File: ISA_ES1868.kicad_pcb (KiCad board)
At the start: 4 copper layers, 104.1 x 99.1 mm, 105 parts, among them J1 LINE IN, J10 Vol. Btns, J11 ISA BUS, J2 LINE OUT, J3 Joystick/MIDI, J5 Wavetable, J7 SPKR OUT, J8 MIC IN, U1 L78L05, U2 74LS138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

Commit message: Fixed silkscreen text
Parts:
- JP3: value ~DRQ2~ Jumper -> DRQ2 Jumper

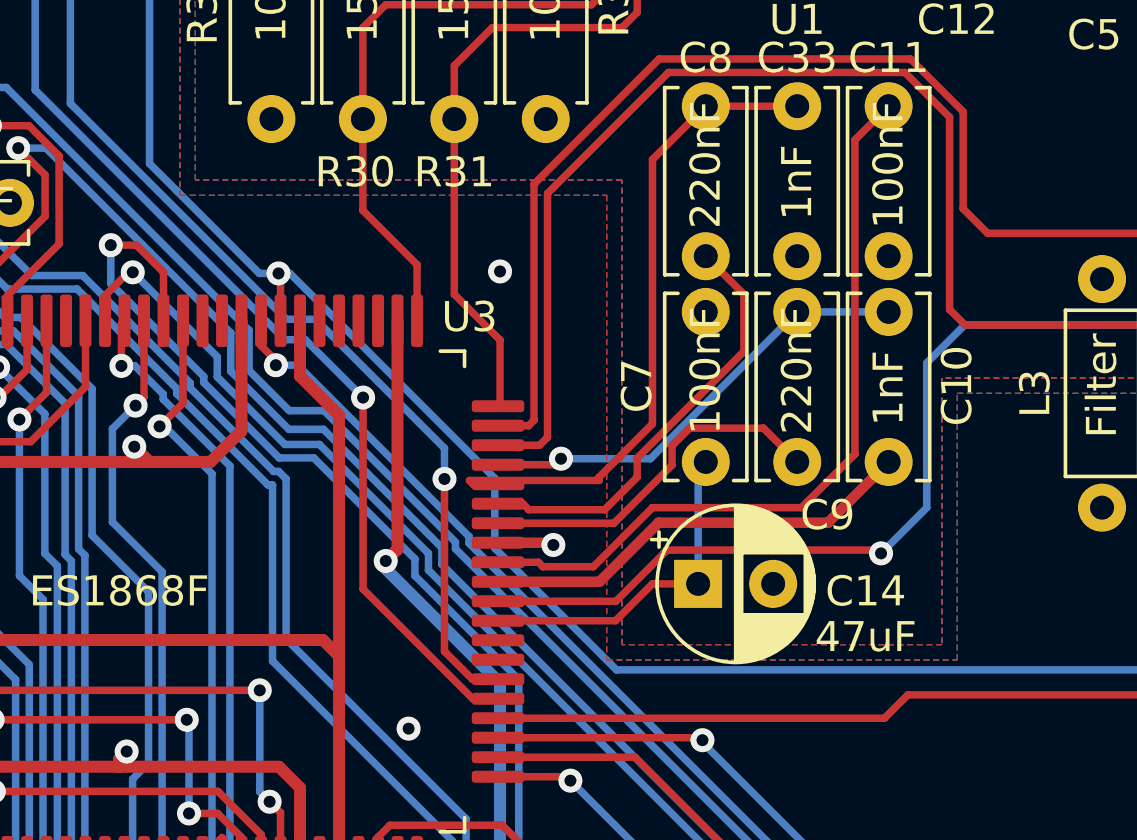
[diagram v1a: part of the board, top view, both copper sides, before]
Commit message: changed analog ground zone
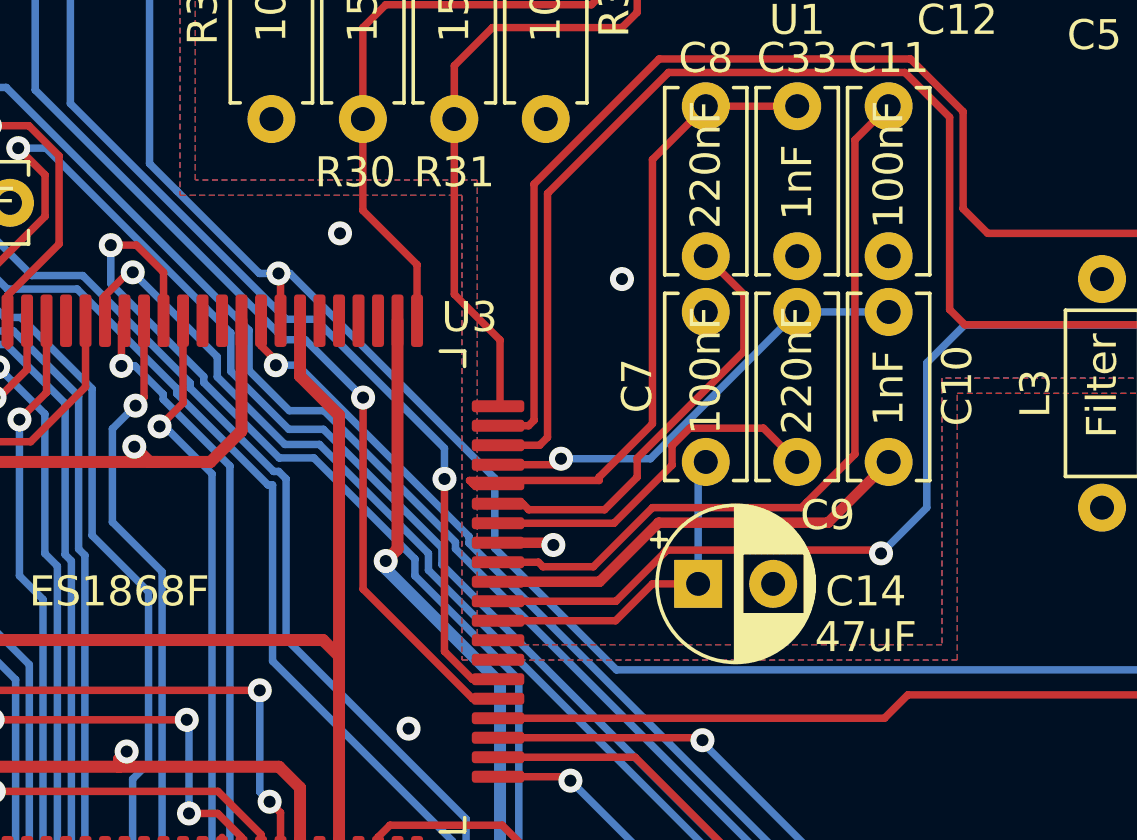
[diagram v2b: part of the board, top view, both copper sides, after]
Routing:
- net GNDA: track 313.7 -> 315.4 mm, vias 2 -> 3
- net GND: track 701.7 -> 702.4 mm

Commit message: Update silkscreen
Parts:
- J5: value Wavetable -> WAVETABLE EXPANSION
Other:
- board text added: "ES1868F ISA8 bit Sound Card by Hkz"
- board text added: "Rev 1.0"
- board text removed: "ES1868F ISA8 bit Sound Card rev. 1.0 by Hkz"

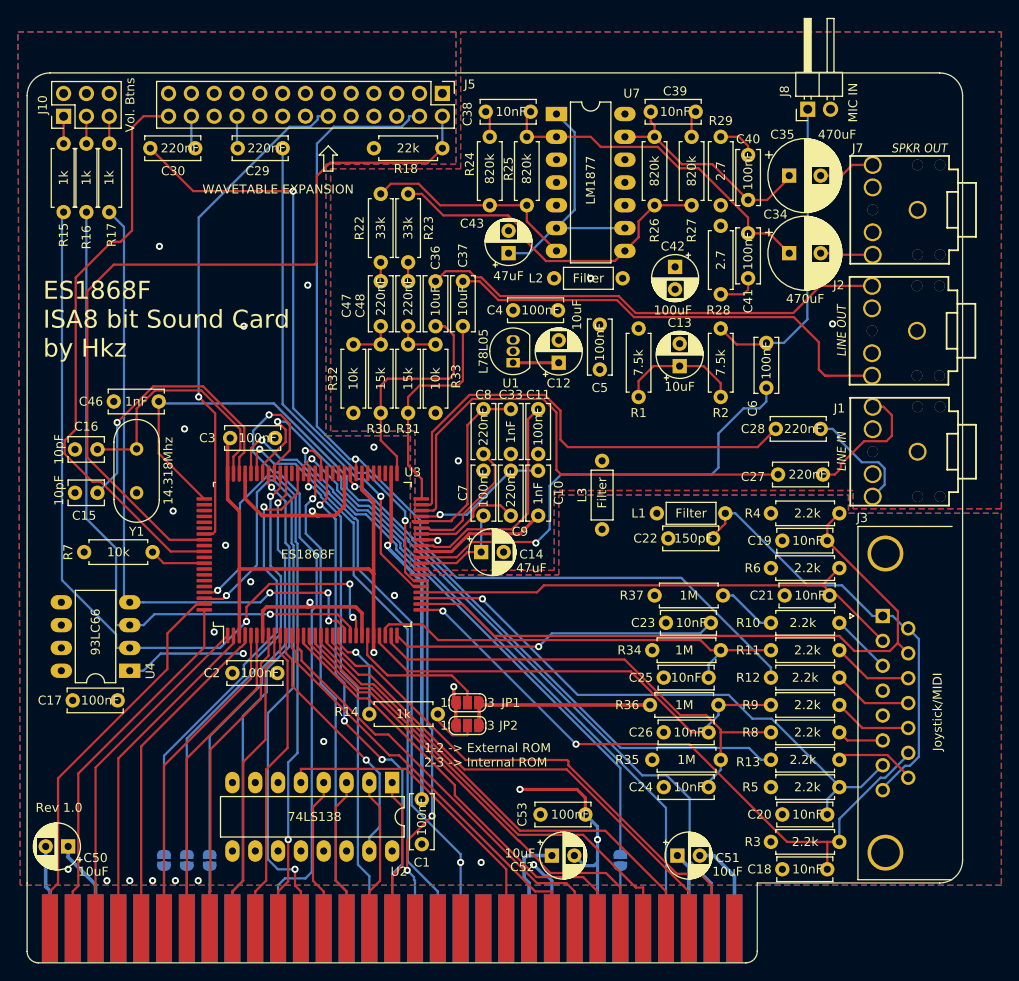
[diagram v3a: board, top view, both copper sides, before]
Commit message: Reorganized crystal on board and moved some traces
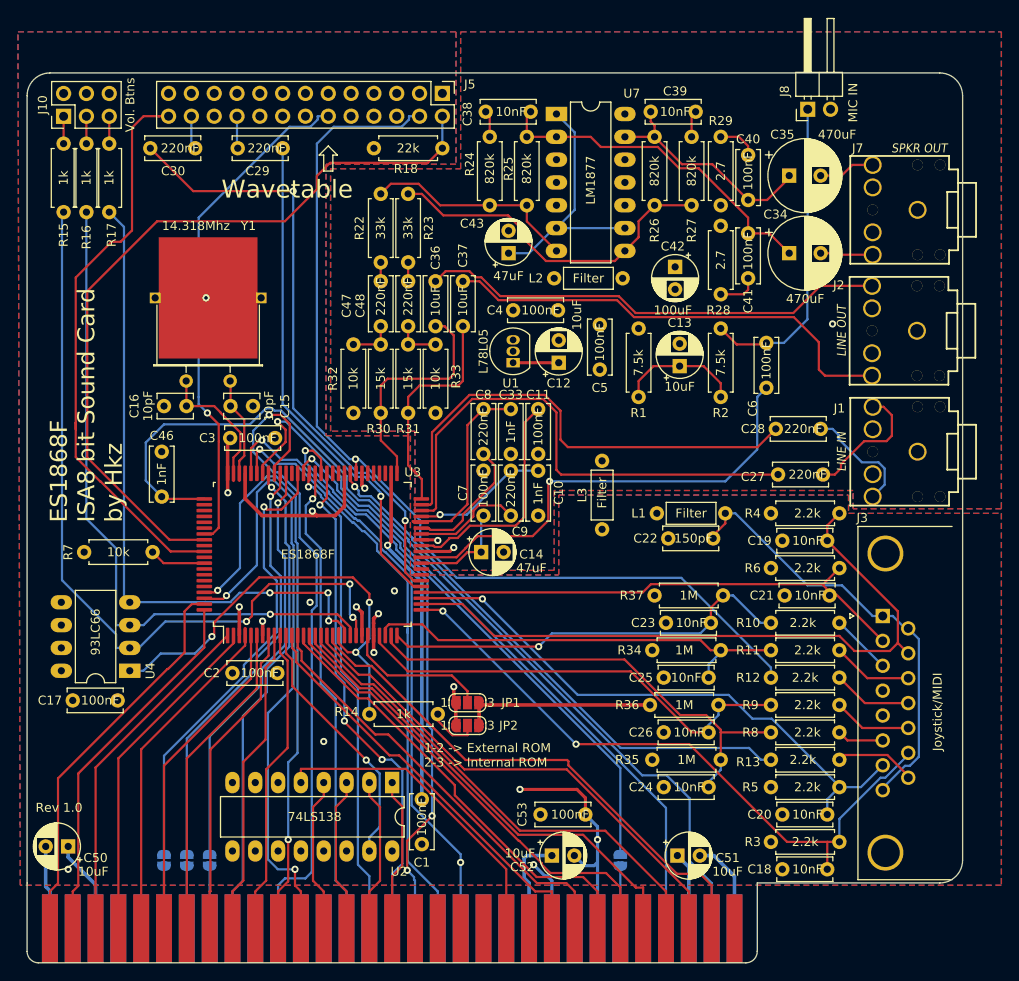
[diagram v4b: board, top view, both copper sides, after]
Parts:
- J5: value WAVETABLE EXPANSION -> Wavetable
- Y1: footprint Crystal:Crystal_HC49-4H_Vertical -> Crystal:Crystal_HC49-U_Horizontal_1EP_style2
- moved C15 22.0 mm to (236.0, 141.2), turned to 180 degrees
- moved Y1 16.2 mm to (233.4, 138.4), turned to 180 degrees
- moved C16 11.0 mm to (226.1, 141.2)
- moved C46 7.73 mm to (225.8, 146.3), turned to 270 degrees
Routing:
- net GND: track 702.4 -> 608.1 mm, vias 21 -> 9
- net Net-(C15-Pad2): track 37.0 -> 12.0 mm, vias 1 -> 0
- net Net-(R14-Pad2): track 37.5 -> 51.2 mm, vias 2 -> 3
- net Net-(C16-Pad2): track 29.1 -> 15.8 mm
- net GNDA: track 315.4 -> 303.6 mm, vias 3 -> 2
- net /MCLK: track 90.7 -> 85.9 mm
- net /RESETDRV: track 106.8 -> 108.1 mm
- net /A0: track 43.7 -> 44.9 mm
- net VCC: track 385.7 -> 384.9 mm, vias 2 -> 6
- net /A4: track 38.3 -> 39.1 mm
- net /~RSTB: track 64.8 -> 64.0 mm
- net Net-(C23-Pad2): track 46.8 -> 47.3 mm
- net /~IOR: track 65.8 -> 66.3 mm

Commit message: Slight change to traces, add gerbers
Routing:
- net GND: track 608.1 -> 629.0 mm, vias 9 -> 11
- net GNDA: track 303.6 -> 306.8 mm, vias 2 -> 3
- net /A3: track 37.9 -> 39.6 mm
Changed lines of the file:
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@@
     (thickness 1.6)
     (drawings 24)
-    (tracks 1401)
+    (tracks 1413)
     (zones 0)
     (modules 105)
@@
     (descr "Crystal THT HC-49/U http://5hertz.com/pdfs/04404_D.pdf")
     (tags "THT crystal")
-    (fp_text reference Y1 (at -2.032 17.272) (layer F.SilkS)
+    (fp_text reference Y1 (at -2.54 0) (layer F.SilkS)
       (effects (font (size 1 1) (thickness 0.15)))
     )
-    (fp_text value 14.318Mhz (at 3.81 17.272 180) (layer F.SilkS)
+    (fp_text value 14.318Mhz (at 9.906 8.89 270) (layer F.SilkS)
       (effects (font (size 1 1) (thickness 0.15)))
     )
@@
   (segment (start 280.162 174.498) (end 261.2081 174.498) (width 0.4) (layer F.Cu) (net 2) (status 30))
   (segment (start 261.2081 174.498) (end 261.142 174.4319) (width 0.4) (layer F.Cu) (net 2) (status 30))
-  (segment (start 216.154 153.416) (end 217.17 154.432) (width 0.4) (layer In1.Cu) (net 2))
-  (segment (start 217.17 154.432) (end 217.17 157.48) (width 0.4) (layer In1.Cu) (net 2) (status 20))
   (segment (start 214.63 165.608) (end 216.154 165.608) (width 0.4) (layer In1.Cu) (net 2) (status 10))
   (segment (start 216.154 165.608) (end 219.202 168.656) (width 0.4) (layer In1.Cu) (net 2))
@@
   (segment (start 249.428 112.522) (end 243.078 112.522) (width 0.4) (layer In1.Cu) (net 2) (status 10))
   (segment (start 243.078 112.522) (end 239.522 116.078) (width 0.4) (layer In1.Cu) (net 2))
-  (segment (start 239.522 116.078) (end 239.522 143.684) (width 0.4) (layer In1.Cu) (net 2))
   (segment (start 239.522 143.684) (end 238.426 144.78) (width 0.4) (layer In1.Cu) (net 2) (status 20))
   (segment (start 267.97 186.69) (end 269.17 187.89) (width 0.4) (layer In1.Cu) (net 2) (status 10))
@@
   (segment (start 247.877799 163.176001) (end 247.877799 162.332201) (width 0.4) (layer In1.Cu) (net 2))
   (segment (start 247.877799 162.332201) (end 247.877799 160.952114) (width 0.4) (layer In1.Cu) (net 2))
+  (segment (start 225.076 129.18) (end 223.372 129.18) (width 0.4) (layer In1.Cu) (net 2))
+  (via (at 219.456 136.906) (size 0.8) (drill 0.4) (layers F.Cu B.Cu) (net 2))
+  (segment (start 219.456 133.096) (end 219.456 136.906) (width 0.4) (layer In1.Cu) (net 2))
+  (segment (start 223.372 129.18) (end 219.456 133.096) (width 0.4) (layer In1.Cu) (net 2))
+  (via (at 225.298 118.11) (size 0.8) (drill 0.4) (layers F.Cu B.Cu) (net 2))
+  (segment (start 225.552 118.364) (end 225.298 118.11) (width 0.4) (layer In1.Cu) (net 2))
+  (segment (start 239.522 118.364) (end 225.552 118.364) (width 0.4) (layer In1.Cu) (net 2))
+  (segment (start 239.522 116.078) (end 239.522 118.364) (width 0.4) (layer In1.Cu) (net 2))
+  (segment (start 239.522 118.364) (end 239.522 143.684) (width 0.4) (layer In1.Cu) (net 2))
   (segment (start 239.738 111.252) (end 239.024 111.252) (width 0.35) (layer In2.Cu) (net 3))
   (segment (start 239.024 111.252) (end 236.728 108.956) (width 0.35) (layer In2.Cu) (net 3) (status 20))
@@
   (segment (start 262.690999 156.304999) (end 263.866 157.48) (width 0.35) (layer In1.Cu) (net 5))
   (segment (start 258.318 156.972) (end 258.985001 156.304999) (width 0.35) (layer In1.Cu) (net 5))
+  (via (at 258.572 148.844) (size 0.8) (drill 0.4) (layers F.Cu B.Cu) (net 5))
+  (segment (start 259 148.416) (end 258.572 148.844) (width 0.35) (layer In1.Cu) (net 5))
+  (segment (start 261.62 148.416) (end 259 148.416) (width 0.35) (layer In1.Cu) (net 5))
   (segment (start 288.036 132.588) (end 289.814 134.366) (width 0.25) (layer F.Cu) (net 6) (status 10))
   (segment (start 289.814 134.366) (end 292.942 134.366) (width 0.25) (layer F.Cu) (net 6) (status 20))
@@
   (segment (start 231.4658 155.459) (end 230.545 155.459) (width 0.25) (layer F.Cu) (net 53))
   (segment (start 232.156 154.7688) (end 231.4658 155.459) (width 0.25) (layer F.Cu) (net 53))
-  (segment (start 232.156 145.175002) (end 232.156 154.7688) (width 0.25) (layer F.Cu) (net 53))
-  (via (at 230.886 141.986) (size 0.8) (drill 0.4) (layers F.Cu B.Cu) (net 53))
-  (segment (start 229.9199 141.0199) (end 230.886 141.986) (width 0.25) (layer B.Cu) (net 53))
   (segment (start 229.9199 140.2068) (end 229.9199 141.0199) (width 0.25) (layer B.Cu) (net 53))
   (segment (start 232.156 143.256) (end 232.156 145.175002) (width 0.25) (layer F.Cu) (net 53))
+  (segment (start 232.156 145.175002) (end 232.156 154.7688) (width 0.25) (layer F.Cu) (net 53))
   (segment (start 230.886 141.986) (end 232.156 143.256) (width 0.25) (layer F.Cu) (net 53))
+  (segment (start 229.9199 141.0199) (end 230.886 141.986) (width 0.25) (layer B.Cu) (net 53))
+  (via (at 230.886 141.986) (size 0.8) (drill 0.4) (layers F.Cu B.Cu) (net 53))
   (segment (start 293.624 170.3247) (end 283.6454 160.3461) (width 0.25) (layer B.Cu) (net 54))
   (segment (start 283.6454 160.3461) (end 258.6401 160.3461) (width 0.25) (layer B.Cu) (net 54))
@@
   (segment (start 218.44 199.39) (end 218.44 181.464) (width 0.25) (layer F.Cu) (net 61) (status 10))
   (segment (start 218.44 181.464) (end 233.145 166.759) (width 0.25) (layer F.Cu) (net 61) (status 20))
-  (segment (start 220.98 199.39) (end 220.98 180.434) (width 0.25) (layer F.Cu) (net 62) (status 10))
-  (segment (start 220.98 180.434) (end 233.795 167.619) (width 0.25) (layer F.Cu) (net 62) (status 20))
   (segment (start 233.795 166.759) (end 233.795 167.619) (width 0.25) (layer F.Cu) (net 62) (status 30))
+  (segment (start 220.98 180.449) (end 220.98 182.118) (width 0.25) (layer F.Cu) (net 62))
+  (segment (start 233.795 167.634) (end 220.98 180.449) (width 0.25) (layer F.Cu) (net 62))
+  (segment (start 233.795 166.759) (end 233.795 167.634) (width 0.25) (layer F.Cu) (net 62))
+  (segment (start 220.98 182.118) (end 220.98 181.356) (width 0.25) (layer F.Cu) (net 62))
+  (segment (start 220.98 199.39) (end 220.98 182.118) (width 0.25) (layer F.Cu) (net 62))
   (segment (start 235.095 166.759) (end 235.095 165.929) (width 0.25) (layer F.Cu) (net 63) (status 30))
   (segment (start 235.095 167.6095) (end 235.095 166.759) (width 0.25) (layer F.Cu) (net 63) (status 30))

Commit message: Changes to gnd plane, redone gerbers
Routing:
- net GND: track 629.0 -> 647.1 mm, vias 11 -> 13

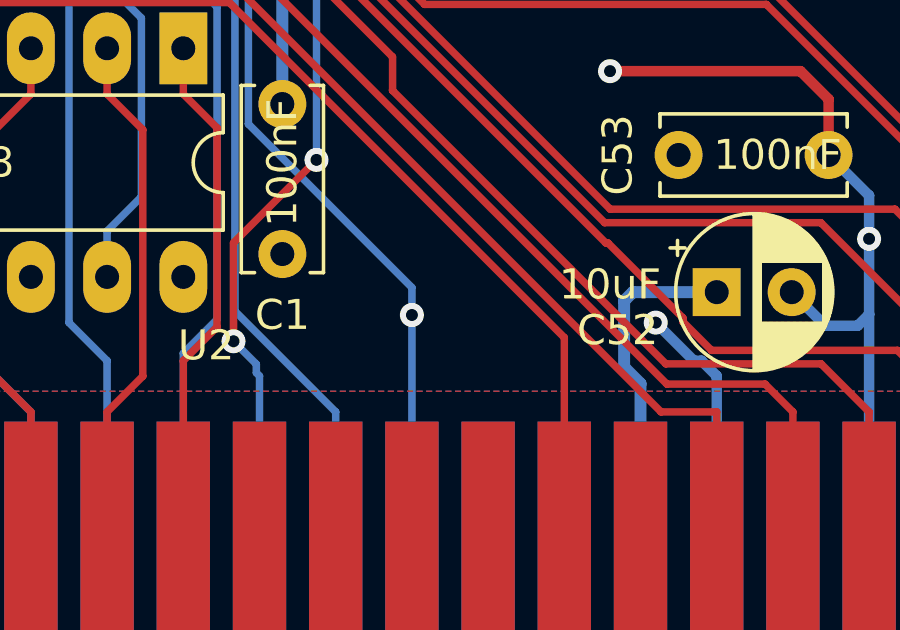
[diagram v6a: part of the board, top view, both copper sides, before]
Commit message: Add more gnd plane, redone gerbers
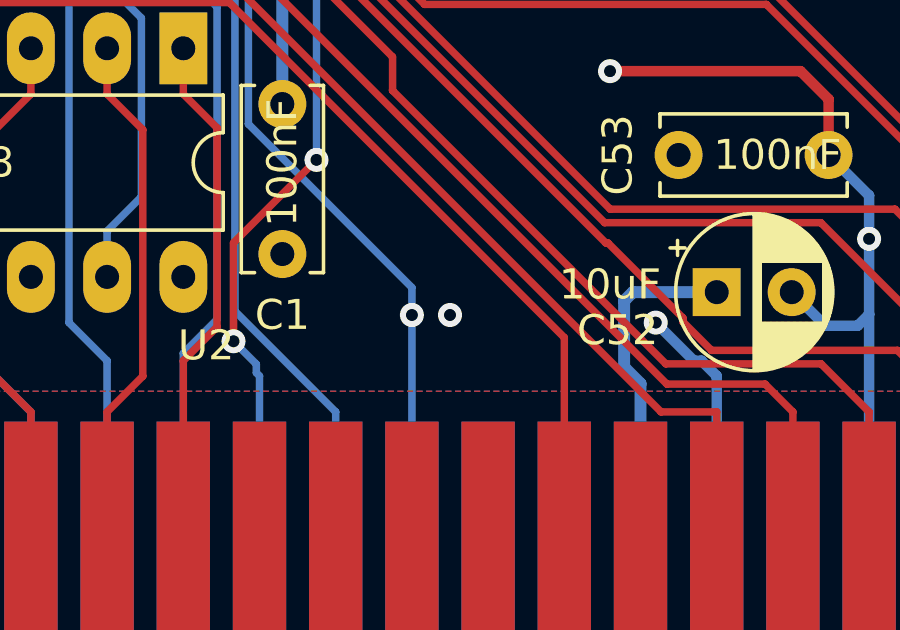
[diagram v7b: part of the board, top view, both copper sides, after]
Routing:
- net GND: track 647.1 -> 657.1 mm, vias 13 -> 14

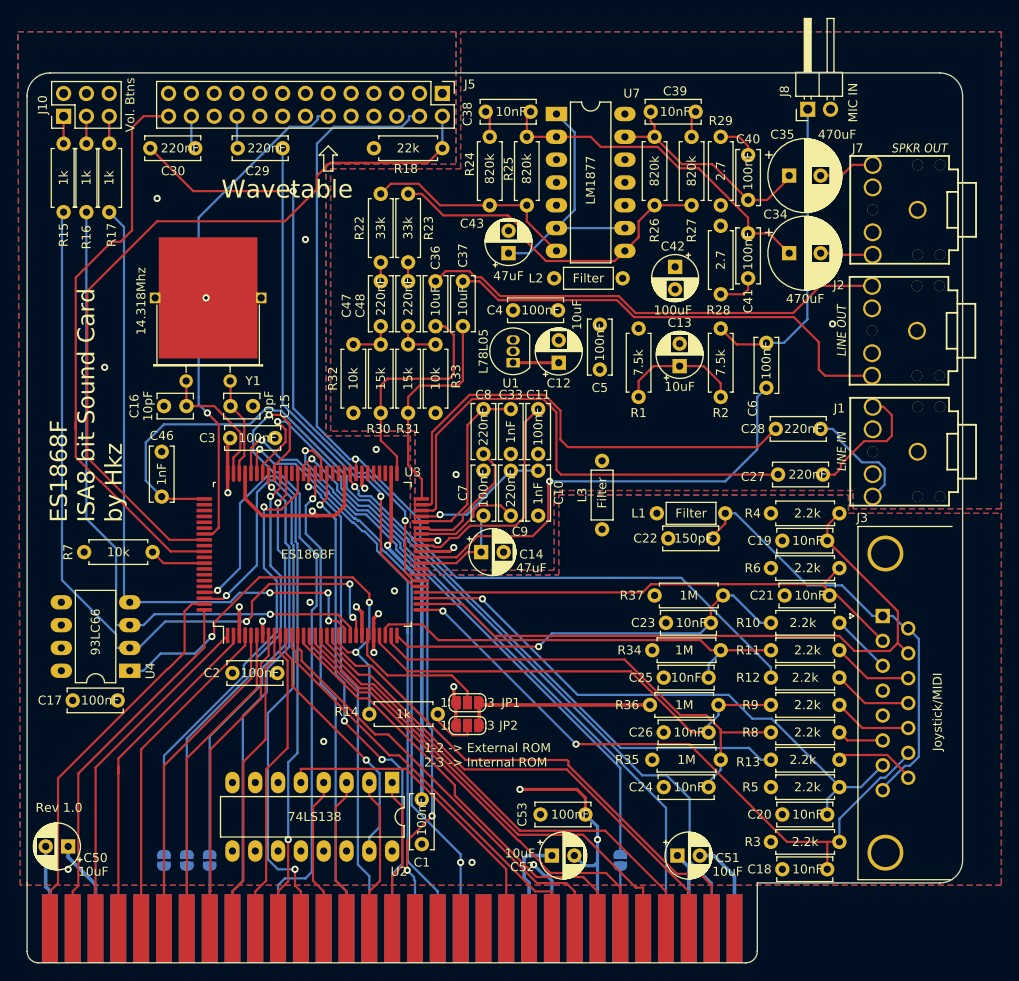
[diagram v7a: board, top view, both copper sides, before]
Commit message: Rerouting some traces
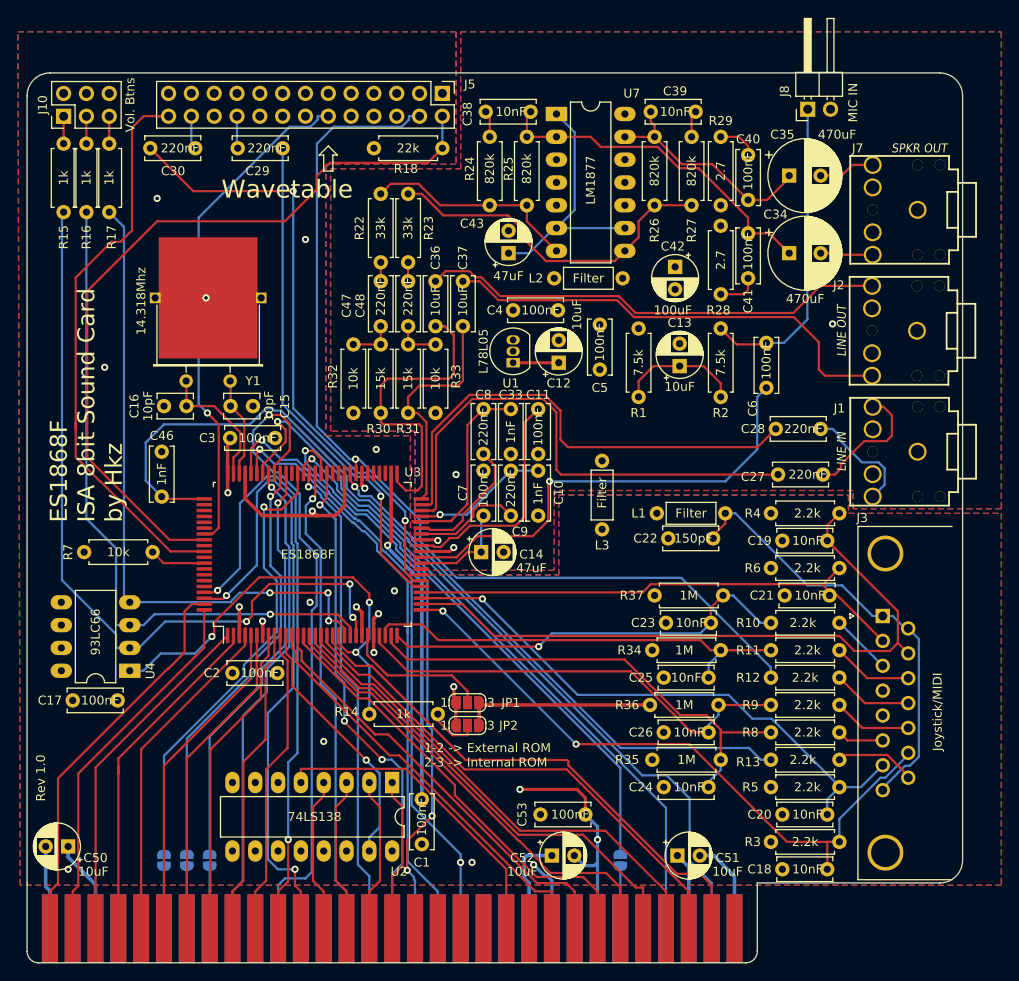
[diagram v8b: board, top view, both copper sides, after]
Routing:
- net /AOUTR: track 25.9 -> 35.2 mm
- net /AOUTL: track 24.9 -> 26.0 mm
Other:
- board text added: "ES1868F ISA 8bit Sound Card by Hkz"
- board text removed: "ES1868F ISA8 bit Sound Card by Hkz"
